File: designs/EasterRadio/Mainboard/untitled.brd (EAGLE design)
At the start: 126 x 58 mm, 7 parts

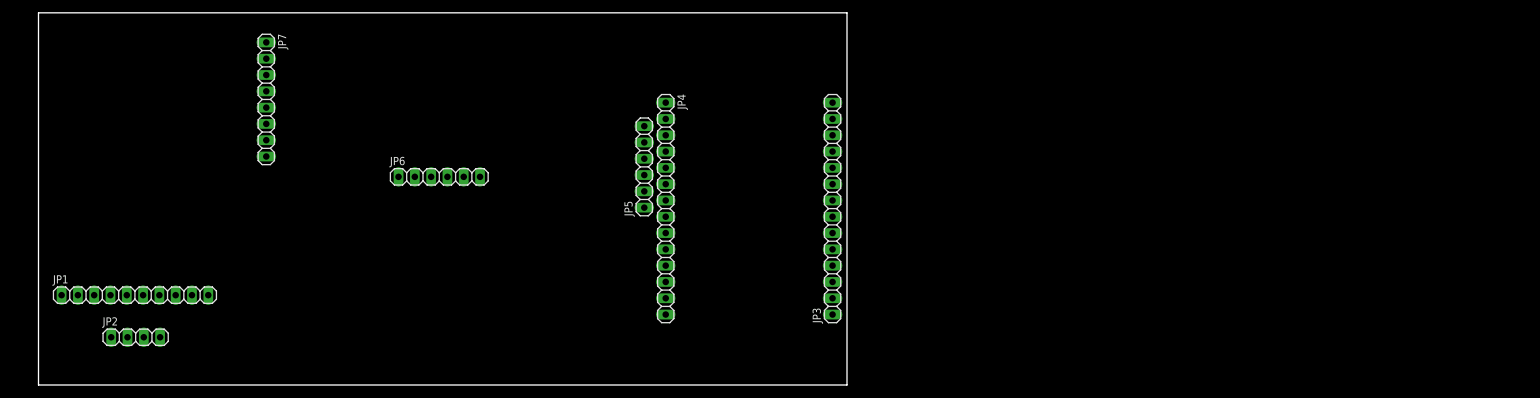
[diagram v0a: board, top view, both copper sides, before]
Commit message: added mainboard layout and new 3.5mm jack
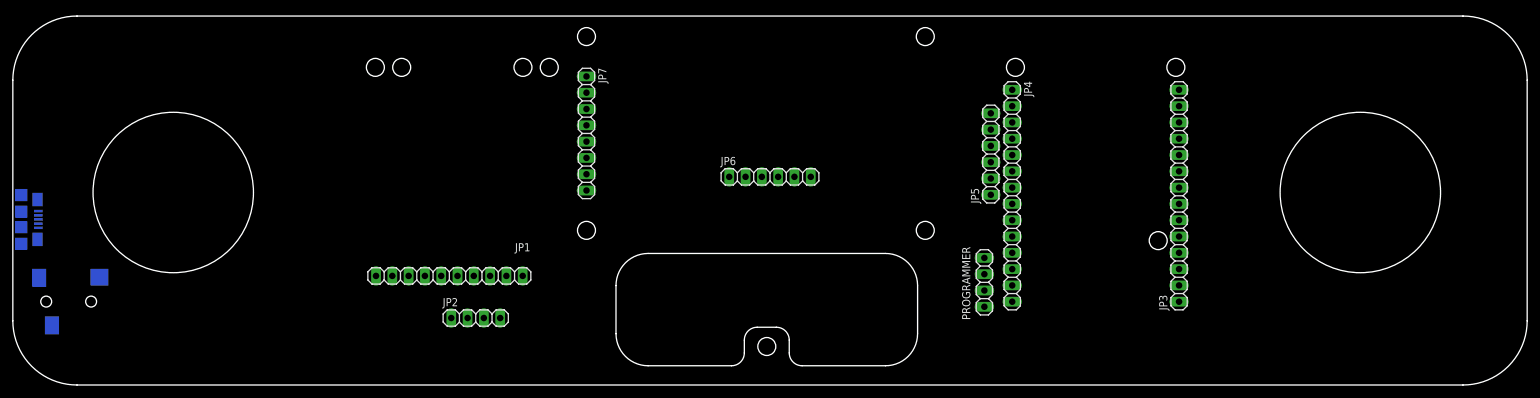
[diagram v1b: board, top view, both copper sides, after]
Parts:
- added J1: 10118192-0001LF, MouserUseful:101181920001LF
- added J2: SJ-3523-SMT-TR, MouserUseful:SJ3523SMTTR
- added PROGRAMMER: (no value), pinhead:1X04
- moved JP3 54.0 mm to (176.8, 29.5)
- moved JP4 54.0 mm to (150.8, 29.5)
- moved JP5 54.0 mm to (147.4, 36.0)
- moved JP2 53.1 mm to (67.1, 10.4)
- moved JP6 51.5 mm to (113.0, 32.4)
- moved JP7 50.2 mm to (84.4, 39.2)
- moved JP1 49.1 mm to (63.0, 17.0)
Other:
- board size 126 x 58 mm -> 236 x 57.5 mm

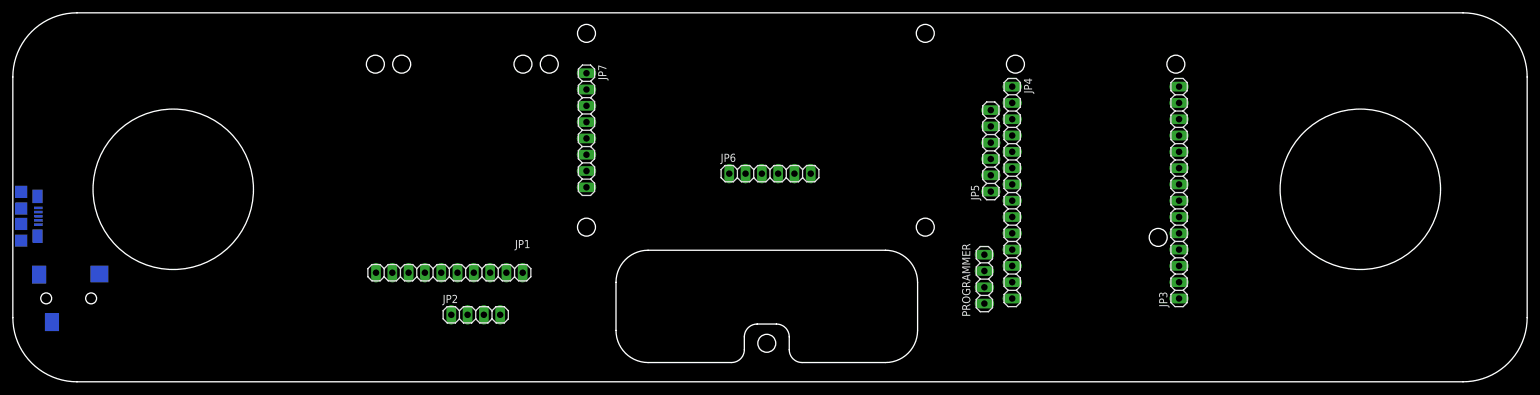
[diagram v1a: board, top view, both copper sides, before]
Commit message: added more stuff to pcb main for radio
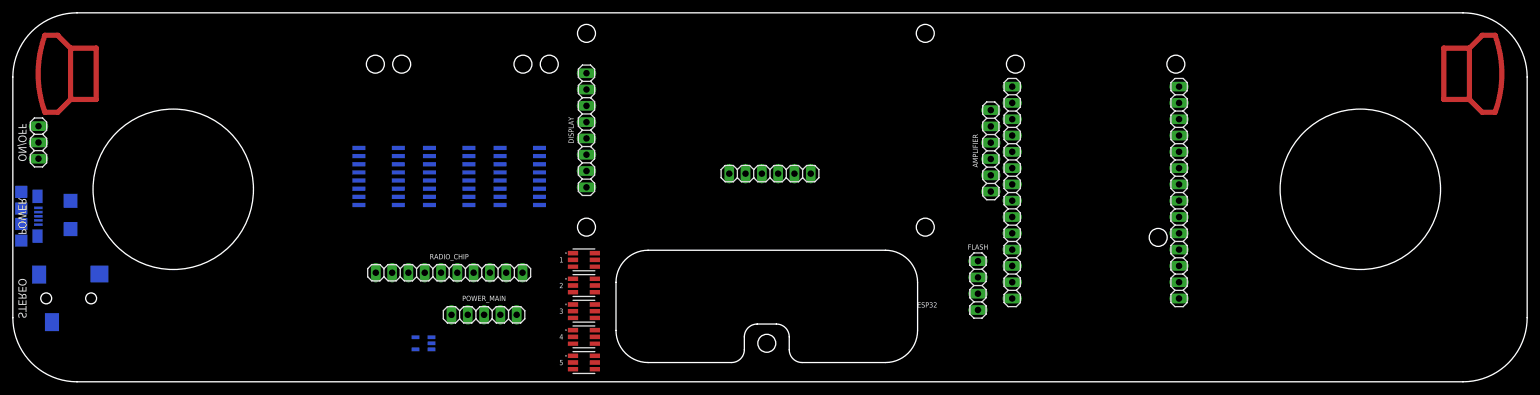
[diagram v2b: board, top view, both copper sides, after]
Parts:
- removed JP1: (no value), pinhead:1X10
- removed JP2, PROGRAMMER: (no value), pinhead:1X04
- added 1, 2, 3, 4, 5: CLY6D-FKC-CK1N1D1BB7D3D3, MouserUseful:PLCC6
- added D1: LSM115JE3_TR13, CommonParts:DIOM5436X330N
- added FLASH: (no value), pinhead:1X04
- added IC1: Analog Digital, MouserUseful:SOT95P280X145-5N
- added IC2, IC3, IC4: 74HC595D, NixieTube:SO16
- added ON/OFF: (no value), pinhead:1X03
- added POWER_MAIN: (no value), pinhead:1X05
- added RADIO_CHIP: (no value), pinhead:1X10
- turned ESP32 to 90 degrees
- turned JP3 to 270 degrees
- renumbered J1 to POWER, J2 to STEREO, JP4 to ESP32, JP5 to AMPLIFIER, JP6 to CONTROL, JP7 to DISPLAY
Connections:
- new net !MUTE: AMPLIFIER.2
- new net !SHDN: AMPLIFIER.3
- new net 3.3V: AMPLIFIER.1, ESP32.13, FLASH.4, IC1.1, ON/OFF.3, POWER_MAIN.5, RADIO_CHIP.10
- new net 5V: D1.1, POWER.1, POWER_MAIN.3
- new net CS: JP3.1
- new net CS2: ESP32.10
- new net DC: JP3.2
- new net EN: ON/OFF.2, POWER_MAIN.4
- new net ENC_1: JP3.6
- new net ENC_2: JP3.7
- new net GND: AMPLIFIER.6, D1.2, ESP32.14, FLASH.3, IC1.2, IC2.8, IC3.8, IC4.8, ON/OFF.1, POWER.5, POWER_MAIN.2, RADIO_CHIP.9, STEREO.1
- new net INL: AMPLIFIER.4, RADIO_CHIP.3, STEREO.2
- new net INR: AMPLIFIER.5, RADIO_CHIP.4, STEREO.3
- new net IO12: ESP32.2
- new net IO13: ESP32.1
- new net IO14: ESP32.3
- new net IO25: ESP32.6
- new net IO26: ESP32.5
- new net IO27: ESP32.4
- new net IO33: ESP32.7
- new net IRQ_RADIO_IC: ESP32.8, RADIO_CHIP.5
- new net MOSI: JP3.5
- new net RST: JP3.3
- new net RST_RADIO_IC: ESP32.9, RADIO_CHIP.8
- new net RXD0: FLASH.2, JP3.9
- new net SCL: IC1.5, JP3.11, RADIO_CHIP.6
- new net SCLK: JP3.4
- new net SDA: IC1.4, JP3.8, RADIO_CHIP.7
- new net SENSOR_VN: ESP32.11
- new net SENSOR_VP: ESP32.12
- new net TUNE1: RADIO_CHIP.1
- new net TUNE2: RADIO_CHIP.2
- new net TXD0: JP3.10
- new net TXDO: FLASH.1
- new net U_DRAIN: IC1.3, POWER_MAIN.1
- new net VCC: IC2.16, IC3.16, IC4.16
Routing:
- net N$2: track 0.00 -> 45.7 mm
- net N$1: track 0.00 -> 45.7 mm
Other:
- board text added: "3.3V"
- board text added: "GND"
- board text added: "Rx"
- board text added: "Tx"

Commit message: started board routing
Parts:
- added D10, D11, D12, D13, D14, D15, D16, D17, D18, D19, D2, D20, D21, D22, D23, D24, D25, D26, D3, D4, D5, D6, D7, D8, D9: PESD3V3L2BT,215, MouserUseful:SOT95P230X110-3N
- added GPIOS: (no value), pinhead:1X04
- POWER: value 10118192-0001LF -> KMMX-BSMT35S-B30TR; device MouserUseful:101181920001LF -> MouserUseful:KMMXBSMT35SB30TR
- moved IC1 0.76 mm to (58.7, 5.30)
- moved POWER 0.45 mm to (-3.10, 26.0)
- turned 1 to 180 degrees
- turned 2 to 180 degrees
- turned 3 to 180 degrees
- turned 4 to 180 degrees
- turned 5 to 180 degrees
- turned CONTROL to 180 degrees
- turned DISPLAY to 90 degrees
- turned JP3 to 90 degrees
- turned POWER_MAIN to 180 degrees
- turned RADIO_CHIP to 180 degrees
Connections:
- removed net IO25: ESP32.6
- removed net IO26: ESP32.5
- removed net IO33: ESP32.7
- removed net VCC: IC2.16, IC3.16, IC4.16
- new net DS: D22.2, ESP32.7, IC2.14
- new net ENC_A: CONTROL.4, D2.2
- new net ENC_B: CONTROL.5, D2.1
- new net N$10: 2.4, IC2.3
- new net N$11: 2.5, IC2.4
- new net N$12: 2.6, IC2.5
- new net N$13: 3.4, IC3.15
- new net N$14: 3.5, IC3.1
- new net N$15: 4.4, IC3.3
- new net N$16: 4.5, IC3.4
- new net N$17: IC2.9, IC3.14
- new net N$18: 5.4, IC4.15
- new net N$19: 5.5, IC4.1
- new net N$21: IC3.9, IC4.14
- new net N$3: 3.6, IC3.2
- new net N$4: 5.6, IC4.2
- new net N$6: 4.6, IC3.5
- new net N$7: 1.4, IC2.15
- new net N$8: 1.5, IC2.1
- new net N$9: 1.6, IC2.2
- new net SHCP: D23.1, ESP32.6, IC2.11, IC3.11, IC4.11
- new net STCP: D23.2, ESP32.5, IC2.12, IC3.12, IC4.12
- net !MUTE: now also D6.1
- net !SHDN: now also D5.2
- net 3.3V: now also CONTROL.3, D14.1, D3.1, DISPLAY.8, IC2.10, IC2.16, IC3.10, IC3.16, IC4.10, IC4.16
- net CS: now also D15.1, DISPLAY.4
- net DC: now also D15.2, DISPLAY.3
- net EN: now also D14.2, D7.2
- net ENC_1: now also D17.2
- net ENC_2: now also D18.1
- net GND: now also 1.1, 1.2, 1.3, 2.1, 2.2, 2.3, 3.1, 3.2, 3.3, 4.1, 4.2, 4.3, 5.1, 5.2, 5.3, CONTROL.6, D10.3, D11.3, D12.3, D13.3, D14.3, D15.3, D16.3, D17.3, D18.3, D19.3, D2.3, D20.3, D21.3, D22.3, D23.3, D24.3, D25.3, D26.3, D3.3, D4.3, D5.3, D6.3, D7.3, D8.3, D9.3, DISPLAY.7, IC2.13, IC3.13, IC4.13
- net INL: now also D12.2, D5.1, D9.1
- net INR: now also D12.1, D4.2, D9.2
- net IO12: now also D25.1, GPIOS.3
- net IO13: now also D25.2, GPIOS.4
- net IO14: now also D24.2, GPIOS.2
- net IO27: now also D24.1, GPIOS.1
- net IRQ_RADIO_IC: now also D11.2, D21.2
- net MOSI: now also D17.1, DISPLAY.6
- net RST: now also D16.1, DISPLAY.2
- net RST_RADIO_IC: now also D21.1
- net RXD0: now also D19.1, D8.1
- net SCL: now also D11.1, D20.1
- net SCLK: now also D16.2, DISPLAY.5
- net SDA: now also D10.2, D18.2
- net SENSOR_VN: now also D26.2
- net SENSOR_VP: now also D26.1
- net TUNE1: now also CONTROL.1, D13.2, D4.1
- net TUNE2: now also CONTROL.2, D13.1, D3.2
- net TXD0: now also D19.2
- net TXDO: now also D8.2
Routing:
- net STCP: track 0.00 -> 192.8 mm
- net SCL: track 0.00 -> 186.8 mm
- net SDA: track 0.00 -> 184.4 mm
- net SHCP: track 0.00 -> 184.2 mm
- net DS: track 0.00 -> 136.6 mm, vias 0 -> 1
- net N$14: track 0.00 -> 113.1 mm, vias 0 -> 1
- net N$3: track 0.00 -> 109.3 mm, vias 0 -> 1
- net N$6: track 0.00 -> 104.3 mm, vias 0 -> 1
- net N$16: track 0.00 -> 103.6 mm, vias 0 -> 1
- net N$15: track 0.00 -> 101.9 mm, vias 0 -> 1
- net N$13: track 0.00 -> 97.0 mm, vias 0 -> 1
- net N$10: track 0.00 -> 48.3 mm, vias 0 -> 1
- net N$12: track 0.00 -> 47.7 mm, vias 0 -> 1
- net N$8: track 0.00 -> 47.4 mm, vias 0 -> 1
- net N$9: track 0.00 -> 47.2 mm, vias 0 -> 1
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
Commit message: finalzed brd layout main pcb
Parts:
- removed FLASH: (no value), pinhead:1X04
- removed POWER_MAIN: (no value), pinhead:1X05
- added D27, D28, D29: PESD3V3L2BT,215, MouserUseful:SOT95P230X110-3N
- added ENERGY: KMMX-BSMT35S-B30TR, MouserUseful:KMMXBSMT35SB30TR
- added PROG: (no value), pinhead:1X04
- D1: value LSM115JE3_TR13 -> PESD3V3L2BT,215; device CommonParts:DIOM5436X330N -> MouserUseful:SOT95P230X110-3N
- D4: value PESD3V3L2BT,215 -> LSM115JE3_TR13; device MouserUseful:SOT95P230X110-3N -> CommonParts:DIOM5436X330N
- GPIOS: device pinhead:1X04 -> pinhead:1X08
- IC1: value Analog Digital -> 74HC595D; device MouserUseful:SOT95P280X145-5N -> NixieTube:SO16
- IC4: value 74HC595D -> Analog Digital; device NixieTube:SO16 -> MouserUseful:SOT95P280X145-5N
- POWER: value KMMX-BSMT35S-B30TR -> (none); device MouserUseful:KMMXBSMT35SB30TR -> pinhead:1X05
- moved D21 113.9 mm to (173.0, 29.5), turned to 180 degrees
- moved D20 113.2 mm to (180.5, 24.5), flipped to the bottom, turned to 180 degrees
- moved D19 107.6 mm to (180.5, 19.5), flipped to the bottom, turned to 180 degrees
- moved D3 101.9 mm to (88.5, 32.0)
- moved D8 101.3 mm to (68.0, 20.5), turned to 90 degrees
- moved D2 98.5 mm to (88.5, 37.0)
- moved D18 96.0 mm to (173.0, 14.0), turned to 180 degrees
- moved D7 91.5 mm to (63.0, 20.5), turned to 90 degrees
- moved D1 86.0 mm to (88.5, 42.0), flipped to the top, turned to 0 degrees
- moved D6 81.6 mm to (58.0, 20.5), turned to 90 degrees
- moved D14 80.1 mm to (143.5, 38.5), turned to 180 degrees
- moved D15 79.3 mm to (143.5, 33.5), turned to 180 degrees
- moved POWER 73.2 mm to (68.4, 10.4), flipped to the top, turned to 180 degrees
- moved D17 72.2 mm to (147.0, 12.5)
- moved D13 59.3 mm to (120.5, 36.5), turned to 90 degrees
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- renumbered 1 to LED5, 2 to LED4, 3 to LED3, 4 to LED2, 5 to LED1, JP3 to JP5, RADIO_CHIP to RADIO_IC
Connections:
- removed net ENC_A: CONTROL.4, D2.2
- removed net ENC_B: CONTROL.5, D2.1
- removed net N$21 (its old number): IC3.9, IC4.14
- removed net TXDO: D8.2, FLASH.1
- new net N$17: IC1.9, IC2.14
- new net N$5: D3.2
- net !MUTE: now also D15.1; no longer D6.1
- net !SHDN: now also D15.2; no longer D5.2
- net 3.3V: now also D12.1, D5.2, GPIOS.7, IC1.10, IC1.16, IC4.1, POWER.5, PROG.4; no longer D14.1, D3.1, FLASH.4, IC1.1, IC4.10, IC4.16, POWER_MAIN.5
- net 5V: now also D4.1, ENERGY.1, POWER.3; no longer D1.1, POWER.1, POWER_MAIN.3
- net CS: now also D18.1, D2.1; no longer D15.1
- net CS2: now also D24.1
- net DC: now also D18.2, D2.2; no longer D15.2
- net DS: now also D25.2, IC1.14; no longer D22.2, IC2.14
- net EN: now also D16.2, D5.1, POWER.4; no longer D14.2, D7.2, POWER_MAIN.4
- net ENC_1: now also CONTROL.4, D11.2, D20.2; no longer D17.2
- net ENC_2: now also CONTROL.5, D11.1, D21.1; no longer D18.1
- net GND: now also D1.3, D27.3, D28.3, D29.3, D4.2, ENERGY.5, GPIOS.8, IC1.13, IC1.8, IC4.2, POWER.2, PROG.3; no longer D1.2, D4.3, FLASH.3, IC1.2, IC4.13, IC4.8, POWER.5, POWER_MAIN.2
- net INL: now also D10.2, D14.1, D8.2; no longer D12.2, D5.1, D9.1
- net INR: now also D10.1, D14.2, D8.1; no longer D12.1, D4.2, D9.2
- net IO12: now also D28.1; no longer D25.1
- net IO13: now also D28.2; no longer D25.2
- net IO14: now also D27.2; no longer D24.2
- net IO27: now also D27.1; no longer D24.1
- net IRQ_RADIO_IC: now also D25.1, D7.2; no longer D11.2, D21.2
- net MOSI: now also D1.1, D20.1; no longer D17.1
- net N$10: now also IC1.3; no longer IC2.3
- net N$11: now also IC1.4; no longer IC2.4
- net N$12: now also IC1.5; no longer IC2.5
- net N$13: now also IC2.15; no longer IC3.15
- net N$14: now also IC2.1; no longer IC3.1
- net N$15: now also IC2.3; no longer IC3.3
- net N$16: now also IC2.4; no longer IC3.4
- net N$18: now also IC3.15; no longer IC4.15
- net N$19: now also IC3.1; no longer IC4.1
- net N$3: now also IC2.2; no longer IC3.2
- net N$4: now also IC3.2; no longer IC4.2
- net N$6: now also IC2.5; no longer IC3.5
- net N$7: now also IC1.15; no longer IC2.15
- net N$8: now also IC1.1; no longer IC2.1
- net N$9: now also IC1.2; no longer IC2.2
- net RST: now also D19.1, D3.1; no longer D16.1
- net RST_RADIO_IC: now also D24.2, D6.1; no longer D21.1
- net RXD0: now also D17.1, D22.1, PROG.2; no longer D19.1, D8.1, FLASH.2
- net SCL: now also D23.1, D7.1, IC4.5; no longer D11.1, D20.1, IC1.5
- net SCLK: now also D1.2, D19.2; no longer D16.2
- net SDA: now also D21.2, D6.2, IC4.4; no longer D10.2, D18.2, IC1.4
- net SENSOR_VN: now also D29.2, GPIOS.6; no longer D26.2
- net SENSOR_VP: now also D29.1, GPIOS.5; no longer D26.1
- net SHCP: now also D26.1, IC1.11; no longer D23.1, IC4.11
- net STCP: now also D26.2, IC1.12; no longer D23.2, IC4.12
- net TUNE1: now also D13.1, D9.2; no longer D13.2, D4.1
- net TUNE2: now also D12.2, D9.1; no longer D13.1, D3.2
- net TXD0: now also D17.2, D22.2, PROG.1; no longer D19.2
- net U_DRAIN: now also IC4.3, POWER.1; no longer IC1.3, POWER_MAIN.1
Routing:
- net 3.3V: track 0.00 -> 400.4 mm, vias 0 -> 13
- net IRQ_RADIO_IC: track 0.00 -> 170.1 mm, vias 0 -> 2
- net INR: track 0.00 -> 169.9 mm, vias 0 -> 6
- net RST_RADIO_IC: track 0.00 -> 168.6 mm, vias 0 -> 2
- net INL: track 0.00 -> 163.8 mm, vias 0 -> 5
- net RST: track 0.00 -> 136.8 mm, vias 0 -> 1
- net CS: track 0.00 -> 136.4 mm
- net DC: track 0.00 -> 135.5 mm, vias 0 -> 2
- net TUNE2: track 0.00 -> 134.2 mm, vias 0 -> 2
- net TUNE1: track 0.00 -> 134.0 mm, vias 0 -> 3
- net SCLK: track 0.00 -> 132.0 mm
- net MOSI: track 0.00 -> 131.6 mm
- net ENC_2: track 0.00 -> 125.0 mm, vias 0 -> 2
- net ENC_1: track 0.00 -> 120.9 mm, vias 0 -> 1
- net 5V: track 0.00 -> 114.4 mm, vias 0 -> 1
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- added copper zone on layer 1, net GND
- added copper zone on layer 16, net GND
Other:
- outline, holes or cut-outs redrawn

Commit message: final changes on mainboard
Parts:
- moved D3 8.14 mm to (80.5, 33.5), turned to 180 degrees
- moved D14 5.10 mm to (142.5, 33.5)
- moved D15 5.10 mm to (142.5, 38.5)
- turned AMPLIFIER to 270 degrees
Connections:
- net !MUTE: now also D15.2; no longer D15.1
- net !SHDN: now also D15.1; no longer D15.2
- net INL: now also D14.2; no longer D14.1
- net INR: now also D14.1; no longer D14.2
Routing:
- net 5V: track 114.4 -> 119.2 mm
- net INR: track 169.9 -> 165.9 mm
- net RST: track 136.8 -> 139.7 mm
- net 3.3V: track 400.4 -> 401.4 mm, vias 13 -> 12
- net INL: track 163.8 -> 162.7 mm
- net !SHDN: track 2.92 -> 3.93 mm
- net !MUTE: track 2.96 -> 3.95 mm
- net SCLK: track 132.0 -> 132.6 mm
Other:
- outline, holes or cut-outs redrawn

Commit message: changed poti and encoder pcb to correct schematic and brd + mainboard change for push btn on rotary encoder
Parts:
- added D30: PESD3V3L2BT,215, MouserUseful:SOT95P230X110-3N
- CONTROL: device pinhead:1X06 -> pinhead:1X07
- moved D11 0.91 mm to (111.4, 36.4)
- moved D12 0.91 mm to (116.4, 36.4)
- moved D13 0.91 mm to (121.4, 36.4)
- moved D27 0.30 mm to (160.6, 8.00)
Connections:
- removed net IO27: D27.1, ESP32.4, GPIOS.1
- new net PUSH: CONTROL.3, D12.1, D30.1, ESP32.4
- net 3.3V: now also CONTROL.7; no longer CONTROL.3, D12.1
- net GND: now also D30.3, GPIOS.1
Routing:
- net PUSH: track 0.00 -> 48.7 mm, vias 0 -> 3
- net IO27: track 27.2 -> 0.00 mm
- net 3.3V: track 401.4 -> 396.9 mm, vias 12 -> 11
- net TUNE2: track 134.2 -> 133.1 mm
- net ENC_2: track 125.0 -> 124.0 mm
- net ENC_1: track 120.9 -> 120.0 mm
